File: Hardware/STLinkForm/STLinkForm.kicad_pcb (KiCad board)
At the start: 2 copper layers, 73.7 x 38.1 mm, 68 parts, among them J1 USB_B_Micro, J2 JTAG, J3 RS232, J4 ISP, J5 SWD, U1 SRV05-4, U2 STM32F103CBT6, U3 HT7833, U4 74LS125, U5 74LS125, U6 AD8531ARTZ, U7 SRV05-4, U8 74LVCH2T45DC, U9 SRV05-4, Y1 8MHz

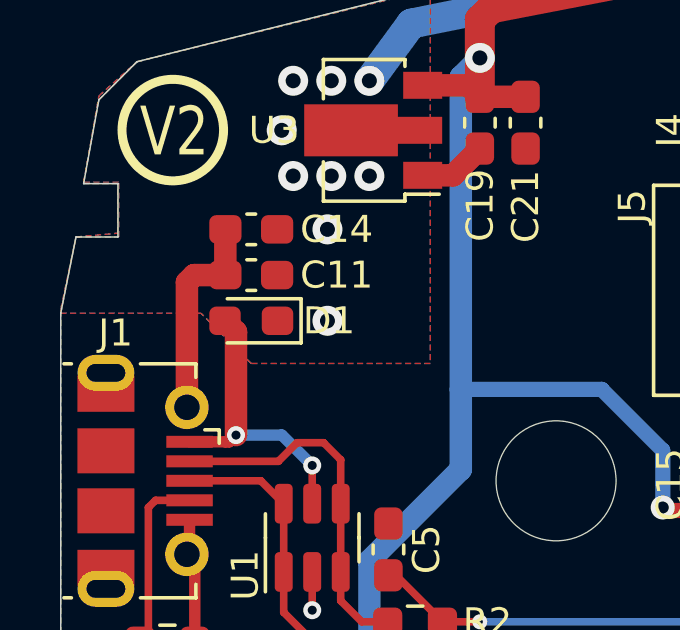
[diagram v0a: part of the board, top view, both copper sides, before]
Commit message: Changed input diode to 1A
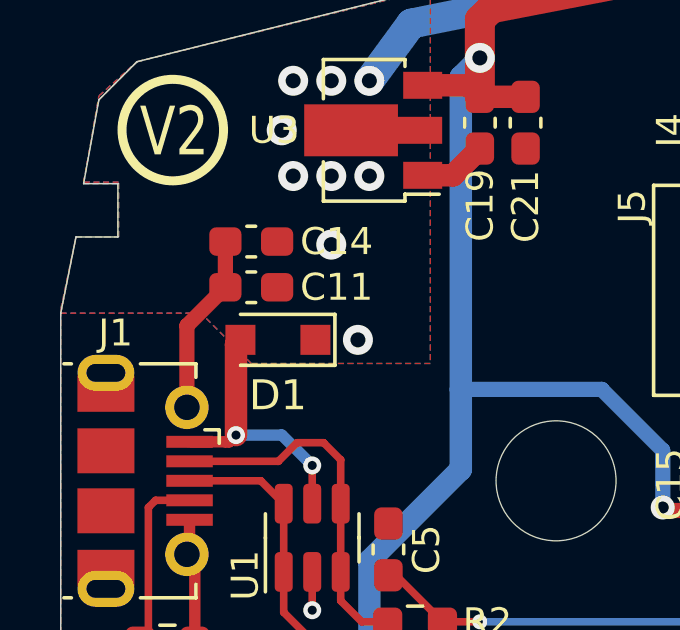
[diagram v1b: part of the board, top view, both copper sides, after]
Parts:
- D1: value CDBURT0530LL -> PMEG4010BEA,115; footprint Diode_SMD:D_0603_1608Metric_Pad1.05x0.95mm_HandSolder -> Diode_SMD:D_SOD-323_HandSoldering
- moved D1 1.09 mm to (70.7, 65.2)
- moved C11 0.41 mm to (69.8, 63.4)
- moved C14 0.41 mm to (69.8, 61.9)
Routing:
- net GND: track 133.8 -> 132.8 mm
- net VBUS: track 9.84 -> 9.11 mm

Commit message: Final review of 'Glossy-MSP430 STLink Form' and fabrication output.
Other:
- rule pad_to_mask_clearance: 0.1 -> 0
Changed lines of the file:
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@@
       (dielectric_constraints no)
     )
-    (pad_to_mask_clearance 0.1)
-    (solder_mask_min_width 0.2)
+    (pad_to_mask_clearance 0)
     (grid_origin 63.5 50.8)
     (pcbplotparams
